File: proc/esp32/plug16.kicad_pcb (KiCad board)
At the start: 2 copper layers, 37.4 x 34.6 mm, 21 parts, among them J7 Moat_Bus_device, Q5 2N7002, U1 VXO78, U2 ESP-32S, U3 P82B96, U4 P82B96

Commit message: esp module update
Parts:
- removed the C5 at (67.5, 43.0)
- removed C7: 100n, Capacitor_SMD:C_0603_1608Metric
- removed J7: Moat_Bus_device, localstuff:Molex_SlimStack_503776-24
- removed JP3, JP4: Jumper_NC, Jumper:SolderJumper-2_P1.3mm_Open_TrianglePad1.0x1.5mm
- removed Q5: 2N7002, Package_TO_SOT_SMD:SOT-23
- removed R4: 10k, Resistor_SMD:R_0603_1608Metric
- removed U4: P82B96, Package_SO:SOIC-8_3.9x4.9mm_P1.27mm
- added C1: 100n, Capacitor_SMD:C_0603_1608Metric, B.Cu at (59.9, 42.3)
- added C2: 100n, Capacitor_SMD:C_0603_1608Metric, B.Cu at (59.9, 46.2)
- added J1: Moat_Bus_device, localstuff:TE_1775013_plug, B.Cu at (33.9, 51.5)
- added Q1: 2N7002, Package_TO_SOT_SMD:SOT-23, B.Cu at (49.9, 42.5)
- added R1: 10k, Resistor_SMD:R_0603_1608Metric, B.Cu at (47.2, 43.2)
- added REF**: OSHW-Logo_5.7x6mm_Copper, Symbol:OSHW-Logo_5.7x6mm_Copper, F.Cu at (51.8, 53.7)
- added U2: P82B96, Package_SO:SOIC-8_3.9x4.9mm_P1.27mm, B.Cu at (64.0, 44.5)
- JP1, JP2: value Jumper_NC -> SolderJumper_3_Bridged12; footprint Jumper:SolderJumper-2_P1.3mm_Open_TrianglePad1.0x1.5mm -> Jumper:SolderJumper-3_P1.3mm_Bridged12_Pad1.0x1.5mm_NumberLabels
- moved JP2 17.9 mm to (54.3, 42.5)
- moved JP1 17.3 mm to (54.3, 45.2), turned to 0 degrees
- moved U3 16.3 mm to (55.6, 44.5)
- moved U5 8.29 mm to (52.6, 60.7)
- moved C3 8.29 mm to (63.9, 63.1)
- moved C4 8.29 mm to (39.9, 60.9)
- moved C5 8.29 mm to (39.9, 68.6)
- moved C6 8.29 mm to (39.9, 65.2)
- moved R2 8.29 mm to (47.1, 47.5)
- moved R5 8.29 mm to (63.9, 66.8)
- moved U1 8.29 mm to (46.9, 60.0)
- moved R3 8.29 mm to (62.9, 49.6)
- moved Prog1 8.29 mm to (51.3, 68.3)
- renumbered C1 to C5, R1 to R5, U2 to U5
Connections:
- JP1 pad 1: /SDA -> Net-(JP1-Pad1)
- JP1 pad 2: /SDA_IN -> /Common bus interface/Bus3_12
- JP2 pad 1: /SCL -> /Bus4
- JP2 pad 2: /SCL_IN -> /Common bus interface/Bus4_12
- Prog1 pad 2: /Rx -> /Tx
- U3 pad 1: /SDA -> /Bus3
- U3 pad 2: /SDA_IN -> Net-(JP1-Pad1)
- U3 pad 3: /SDA_IN -> Net-(JP1-Pad1)
- U3 pad 5: /SCL_IN -> Net-(JP2-Pad3)
- U3 pad 6: /SCL_IN -> Net-(JP2-Pad3)
- U3 pad 7: /SCL -> /Bus4
- U5 pad 24: /1w -> /1wire
- U5 pad 25: /RXD2 -> /Rx2
- U5 pad 27: /TXD2 -> /Tx2
- U5 pad 34: /SDA -> /Bus2
- U5 pad 35: /SCL -> /Bus1
- U5 pad 38: /BUS4 -> /Bus4
- U5 pad 41: /Rx -> /Tx
- U5 pad 42: /BUS3 -> /Bus3
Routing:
- net /Rx: track 96.8 -> 45.9 mm, vias 8 -> 4
- net /Tx: track 0.00 -> 43.7 mm, vias 0 -> 4
- net /Common bus interface/Bus2_12: track 0.00 -> 39.4 mm, vias 0 -> 2
- net /Common bus interface/Bus1_12: track 0.00 -> 39.1 mm, vias 0 -> 2
- net /SDA_IN: track 37.3 -> 0.00 mm, vias 2 -> 0
- net /SCL_IN: track 35.6 -> 0.00 mm, vias 2 -> 0
- net /Tx2: track 0.00 -> 28.1 mm, vias 0 -> 2
- net /RXD2: track 27.6 -> 0.00 mm, vias 2 -> 0
- net /TXD2: track 27.3 -> 0.00 mm
- net /Rx2: track 0.00 -> 27.3 mm, vias 0 -> 2
- net /BUS4_IN: track 26.6 -> 0.00 mm, vias 2 -> 0
- net /SCL: track 25.2 -> 0.00 mm, vias 3 -> 0
- net /Bus4: track 0.00 -> 25.0 mm, vias 0 -> 2
- net /BUS3_IN: track 24.9 -> 0.00 mm, vias 2 -> 0
- net /Bus3: track 0.00 -> 24.1 mm, vias 0 -> 2
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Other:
- board size 37.4 x 34.6 mm -> 37.3 x 31.6 mm
- board text added: "3"
- board text added: "4"
- board text added: "V 2.2"
- board text removed: "V 1.1"

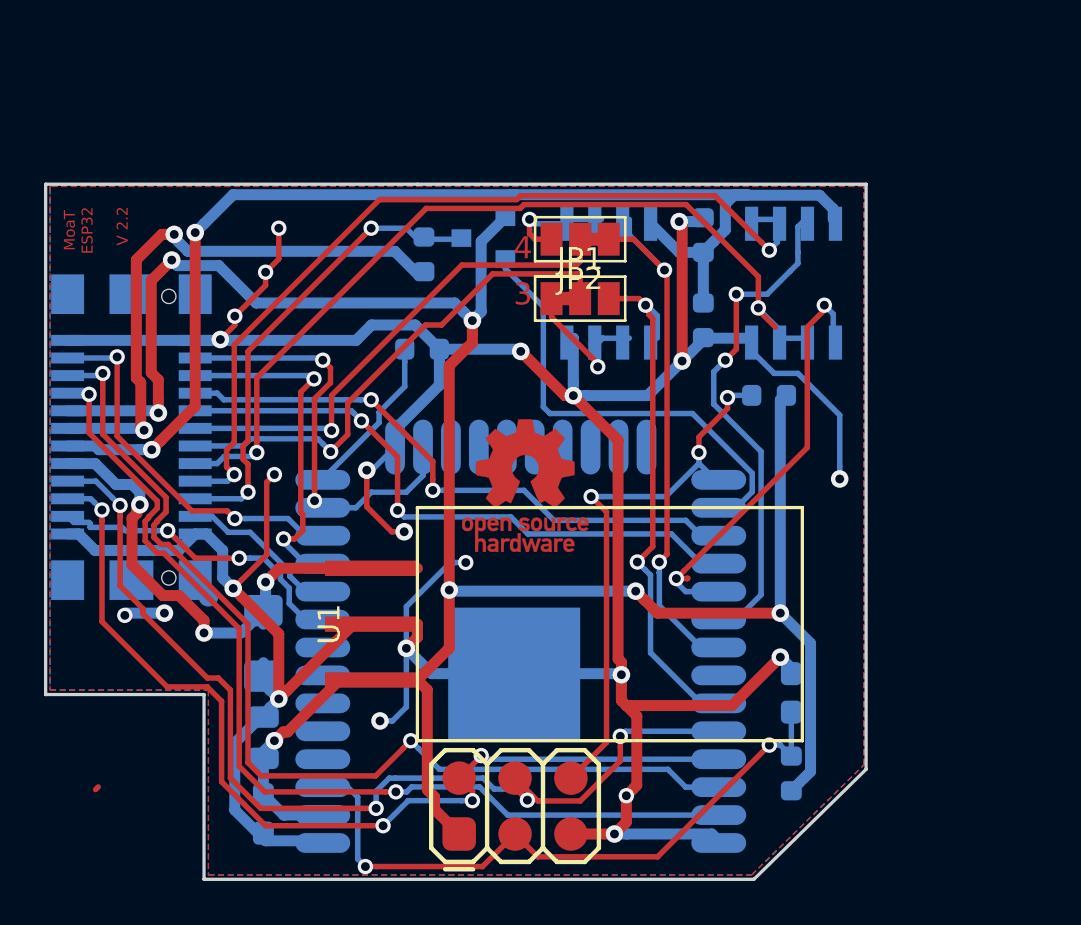
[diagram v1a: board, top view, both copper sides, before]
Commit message: Too many reworks to count.
Most notably: Split GND and GNDPWR.
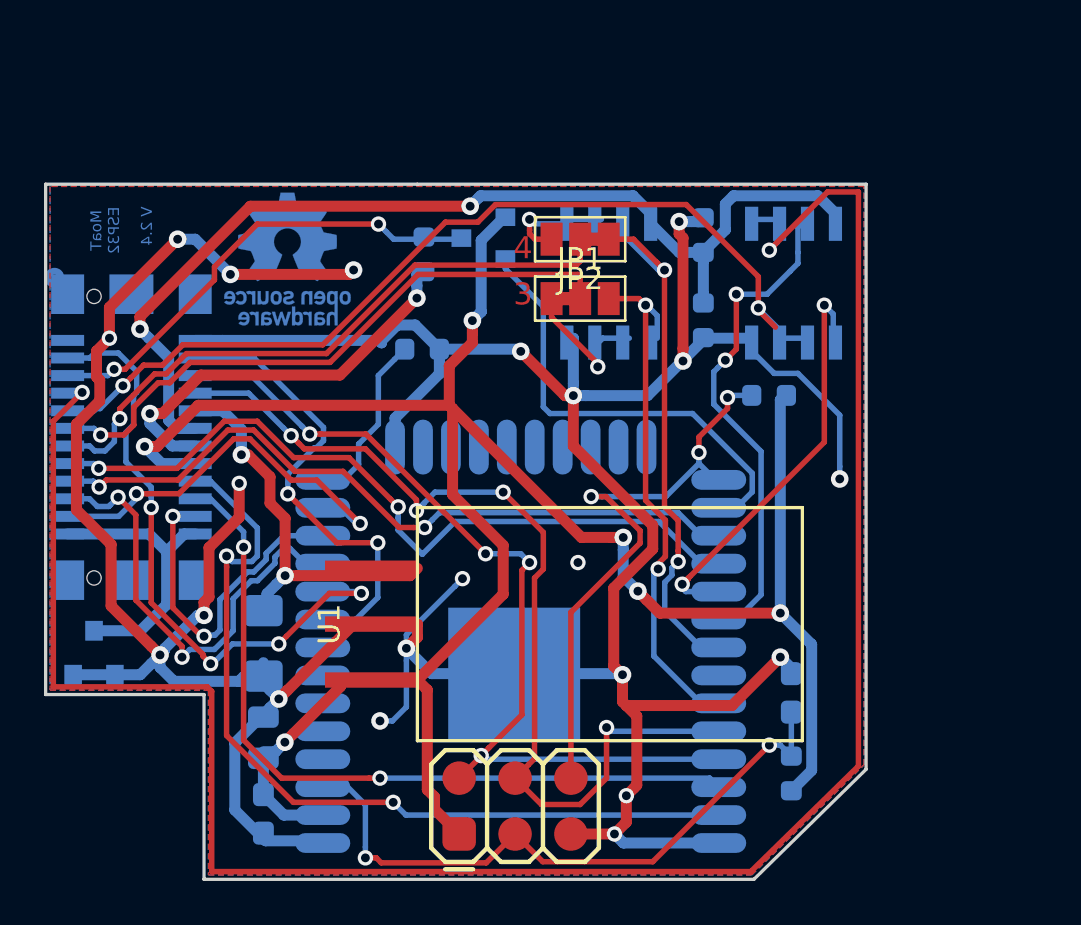
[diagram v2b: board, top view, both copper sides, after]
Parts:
- added D1: D_Schottky_x2_Serial_ACK, Package_TO_SOT_SMD:SOT-23, B.Cu at (32.2, 61.3)
- REF**: moved to B.Cu
- moved REF** 14.9 mm to (41.0, 43.4), turned to 180 degrees
- turned J1 to 90 degrees
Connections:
- J1 pad 23: GND -> GNDPWR
- J1 pad 24: GND -> GNDPWR
- U5 pad 10: Net-(U5-Pad10) -> (no net)
- U5 pad 11: Net-(U5-Pad11) -> (no net)
- U5 pad 12: Net-(U5-Pad12) -> (no net)
- U5 pad 20: /T1 -> (no net)
- U5 pad 21: Net-(U5-Pad21) -> (no net)
- U5 pad 22: Net-(U5-Pad22) -> (no net)
- U5 pad 28: Net-(U5-Pad28) -> (no net)
- U5 pad 29: Net-(U5-Pad29) -> (no net)
- U5 pad 30: Net-(U5-Pad30) -> (no net)
- U5 pad 31: Net-(U5-Pad31) -> (no net)
- U5 pad 32: Net-(U5-Pad32) -> (no net)
- U5 pad 33: Net-(U5-Pad33) -> (no net)
- U5 pad 5: Net-(U5-Pad5) -> (no net)
- U5 pad 8: Net-(U5-Pad8) -> (no net)
- U5 pad NC: Net-(U5-PadNC) -> (no net)
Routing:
- net /Common bus interface/Bus1_12: track 39.1 -> 95.5 mm
- net /SW1: track 7.33 -> 28.6 mm, vias 0 -> 4
- net GNDPWR: track 0.00 -> 12.7 mm
- net GND: track 169.9 -> 181.8 mm
- net /SDAx: track 45.9 -> 34.8 mm
- net +12V: track 54.9 -> 47.3 mm
- net /SW2: track 14.2 -> 21.3 mm
- net +5V: track 25.5 -> 18.4 mm
- net /Tx2: track 28.1 -> 35.1 mm
- net +24V: track 25.0 -> 18.6 mm, vias 3 -> 2
- net /Rx2: track 27.3 -> 33.3 mm
- net /Common bus interface/Bus4_12: track 22.7 -> 28.7 mm
- net /SCLx: track 44.3 -> 38.6 mm
- net /Common bus interface/Bus3_12: track 23.1 -> 28.0 mm
- net /T3: track 16.0 -> 20.8 mm
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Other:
- net class Power: clearance 0.15 -> 0.2
- board text added: "V 2.4"
- board text removed: "V 2.2"
